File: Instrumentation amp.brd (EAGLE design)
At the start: 35.9 x 22.7 mm, 16 parts

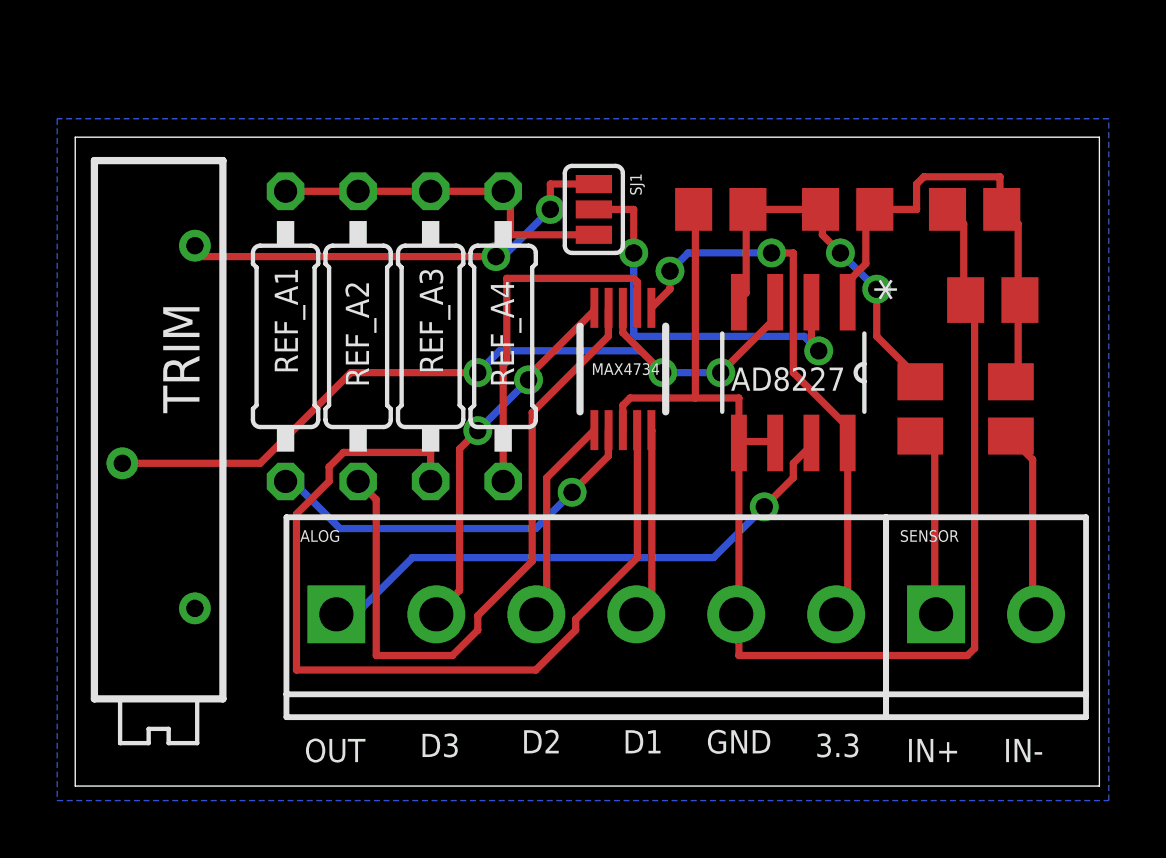
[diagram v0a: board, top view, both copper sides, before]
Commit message: Improved tracing and changes for OSH Park compliance
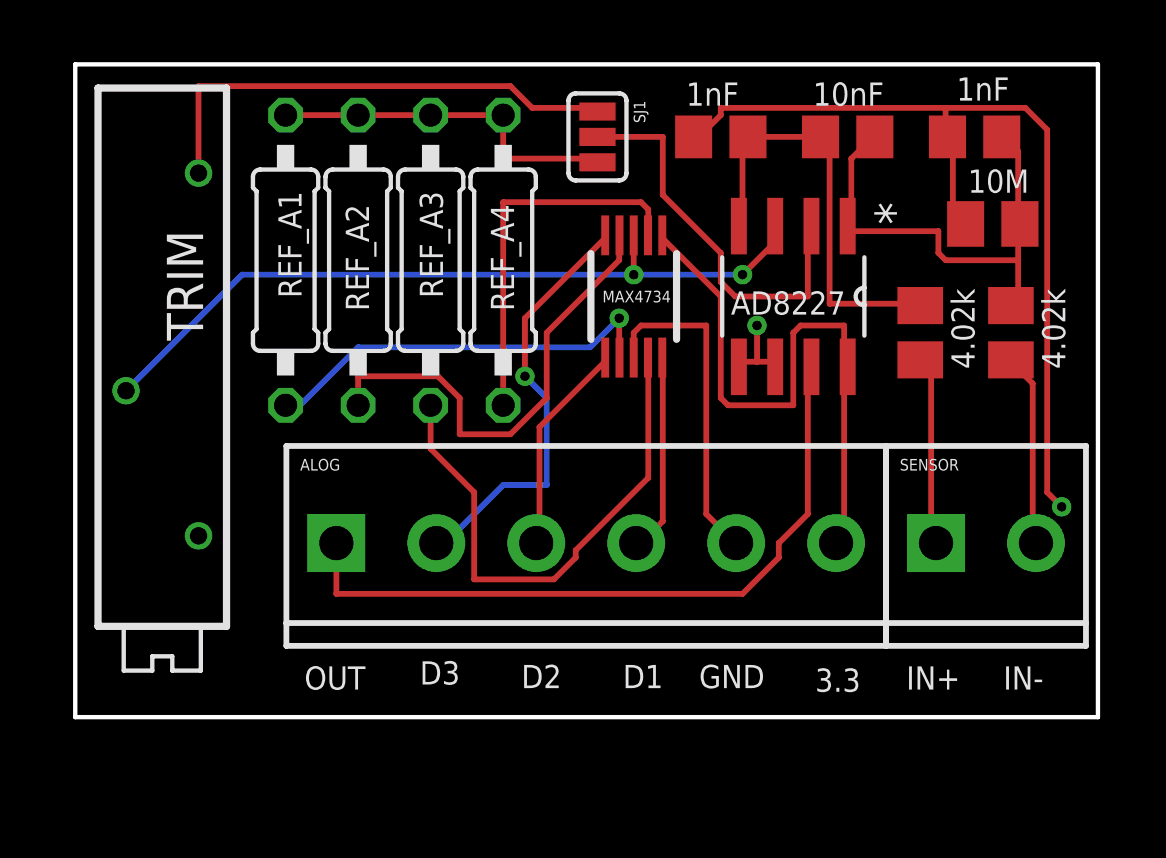
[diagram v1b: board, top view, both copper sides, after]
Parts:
- moved AD8227 2.67 mm to (25.1, 14.7)
- moved R1 2.67 mm to (32.8, 13.5)
- moved R2 2.67 mm to (29.6, 13.5)
- moved R3 2.67 mm to (32.1, 17.3)
- moved REF_A1 2.67 mm to (7.37, 16.0)
- moved REF_A2 2.67 mm to (9.91, 16.0)
- moved REF_A3 2.67 mm to (12.4, 16.0)
- moved REF_A4 2.67 mm to (15.0, 16.0)
- moved U$1 2.57 mm to (19.6, 14.7)
- moved SJ1 2.54 mm to (18.3, 20.3)
- moved TRIM 2.54 mm to (3.05, 11.4)
- moved C1 2.54 mm to (31.5, 20.3)
- moved C2 2.54 mm to (22.6, 20.3)
- moved C3 2.54 mm to (27.1, 20.3)
- moved ALOG 2.50 mm to (9.14, 6.10)
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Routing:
- net N$5: track 30.6 -> 18.7 mm
- net N$6: track 23.5 -> 16.5 mm
- net OUT: track 19.5 -> 25.0 mm, vias 1 -> 0
- net COM: track 29.0 -> 26.8 mm, vias 3 -> 2
- net D3: track 13.0 -> 14.9 mm, vias 2 -> 1
- net +3V3: track 19.7 -> 21.5 mm, vias 2 -> 0
- net N$2: track 13.5 -> 15.1 mm, vias 2 -> 0
- net N$12: track 15.9 -> 17.5 mm, vias 2 -> 0
- net GND: track 46.4 -> 45.6 mm, vias 0 -> 2
- net N$9: track 12.7 -> 13.2 mm
- net N$13: track 14.3 -> 14.0 mm, vias 2 -> 0
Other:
- board size 35.9 x 22.7 mm -> 35.8 x 22.9 mm

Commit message: Changed ground, added ground fill to top layer
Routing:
- net GND: track 45.6 -> 0.44 mm, vias 2 -> 3
- added copper zone on layer 1, net GND
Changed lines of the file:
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@@
 <vertex x="35.814" y="22.86"/>
 </polygon>
-<wire x1="24.384" y1="12.446" x2="23.876" y2="12.446" width="0.2032" layer="1"/>
-<wire x1="23.876" y1="12.446" x2="23.368" y2="12.446" width="0.2032" layer="1"/>
 <wire x1="23.368" y1="12.446" x2="23.241" y2="12.2682" width="0.2032" layer="1"/>
 <wire x1="24.384" y1="12.446" x2="24.511" y2="12.2682" width="0.2032" layer="1"/>
-<wire x1="19.558" y1="13.462" x2="19.558" y2="12.592" width="0.2032" layer="1"/>
-<wire x1="19.812" y1="13.716" x2="19.558" y2="13.462" width="0.2032" layer="1"/>
-<wire x1="22.098" y1="13.716" x2="19.812" y2="13.716" width="0.2032" layer="1"/>
-<wire x1="22.098" y1="7.112" x2="22.098" y2="13.716" width="0.2032" layer="1"/>
-<wire x1="23.114" y1="6.096" x2="22.098" y2="7.112" width="0.2032" layer="1"/>
-<wire x1="23.114" y1="6.096" x2="23.144" y2="6.096" width="0.2032" layer="1"/>
-<wire x1="23.876" y1="13.716" x2="23.876" y2="12.446" width="0.2032" layer="1"/>
-<wire x1="22.606" y1="21.082" x2="21.844" y2="20.32" width="0.2032" layer="1"/>
-<wire x1="22.606" y1="21.336" x2="22.606" y2="21.082" width="0.2032" layer="1"/>
-<wire x1="30.48" y1="21.336" x2="22.606" y2="21.336" width="0.2032" layer="1"/>
-<wire x1="30.48" y1="20.32" x2="30.48" y2="21.336" width="0.2032" layer="1"/>
-<wire x1="21.844" y1="20.32" x2="21.656" y2="20.32" width="0.2032" layer="1"/>
-<wire x1="30.48" y1="20.32" x2="30.546" y2="20.32" width="0.2032" layer="1"/>
-<wire x1="30.734" y1="17.526" x2="30.988" y2="17.272" width="0.2032" layer="1"/>
-<wire x1="30.734" y1="20.32" x2="30.734" y2="17.526" width="0.2032" layer="1"/>
-<wire x1="30.988" y1="17.272" x2="31.181" y2="17.272" width="0.2032" layer="1"/>
-<wire x1="30.734" y1="20.32" x2="30.546" y2="20.32" width="0.2032" layer="1"/>
-<wire x1="34.036" y1="7.874" x2="34.544" y2="7.366" width="0.2032" layer="1"/>
-<wire x1="34.036" y1="20.574" x2="34.036" y2="7.874" width="0.2032" layer="1"/>
-<wire x1="33.274" y1="21.336" x2="34.036" y2="20.574" width="0.2032" layer="1"/>
-<wire x1="30.48" y1="21.336" x2="33.274" y2="21.336" width="0.2032" layer="1"/>
-<via x="23.876" y="13.716" extent="1-16" drill="0.3302"/>
-<via x="34.544" y="7.366" extent="1-16" drill="0.3302"/>
+<polygon width="0.4064" layer="1">
+<vertex x="36.068" y="23.114"/>
+<vertex x="-0.254" y="23.114"/>
+<vertex x="-0.254" y="-0.254"/>
+<vertex x="36.068" y="-0.254"/>
+</polygon>
+<via x="18.034" y="8.89" extent="1-16" drill="0.3302" shape="octagon"/>
+<via x="29.21" y="18.542" extent="1-16" drill="0.3302" shape="octagon"/>
+<via x="23.876" y="13.97" extent="1-16" drill="0.3302" shape="octagon"/>
 </signal>
 <signal name="N$1">
